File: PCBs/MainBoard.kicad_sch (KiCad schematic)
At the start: 47 parts, among them J1 USB_C_Receptacle, J2 Conn_01x12_FPC_0.5mm, J3 Conn_01x08, J4 Qwiic_RA, J5 SM06B-GHS-TB, SW1 PTH_RA_h7.5mm, SW2 SMD_4.6x2.8mm_h2.5mm, SW3 SMD_4.6x2.8mm_h2.5mm, U1 TVS_ESD_USB, U2 ESP32-S3-MINI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

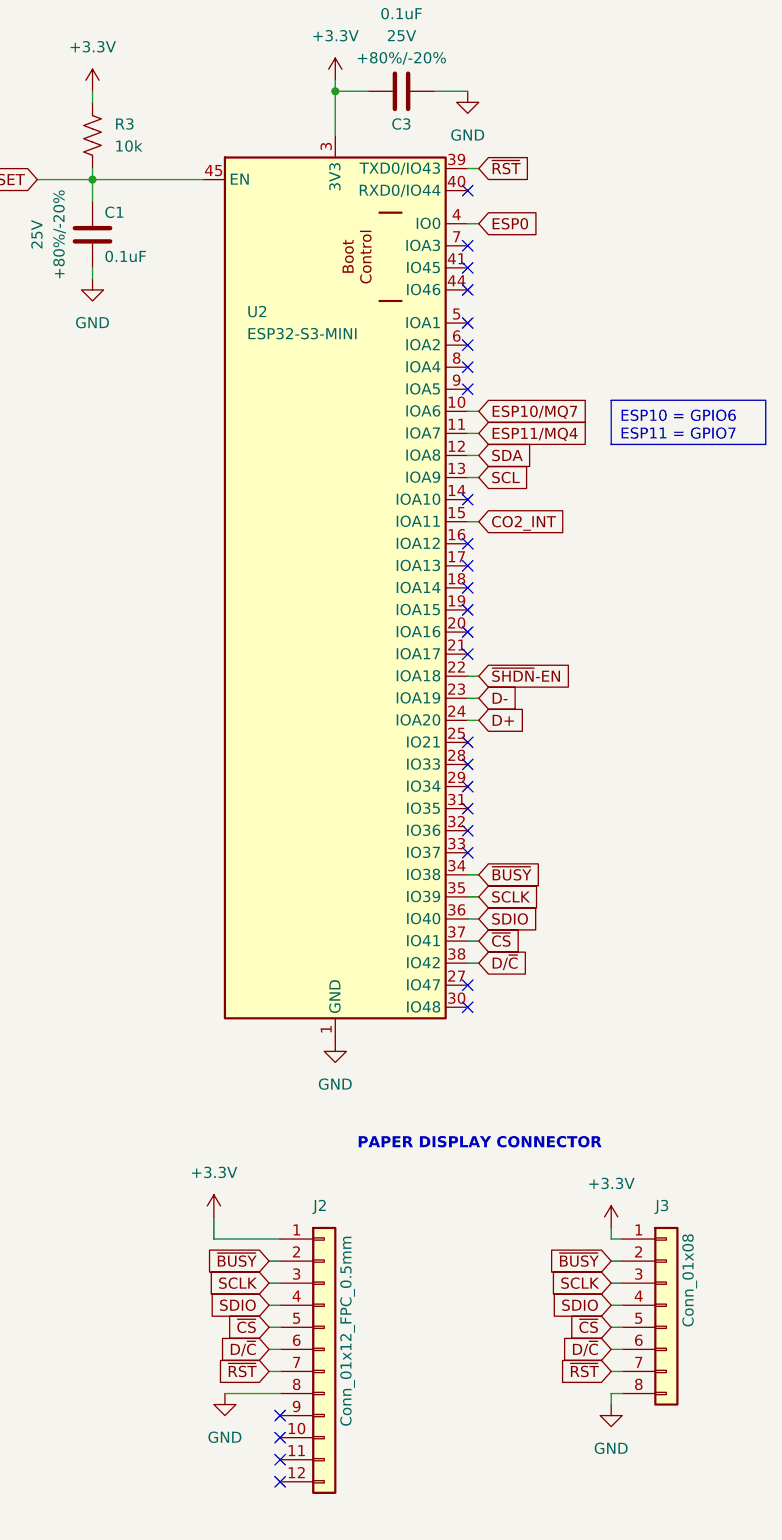
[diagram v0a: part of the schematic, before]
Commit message: Updates
Fixing connections between epaper display board and main board pcbs
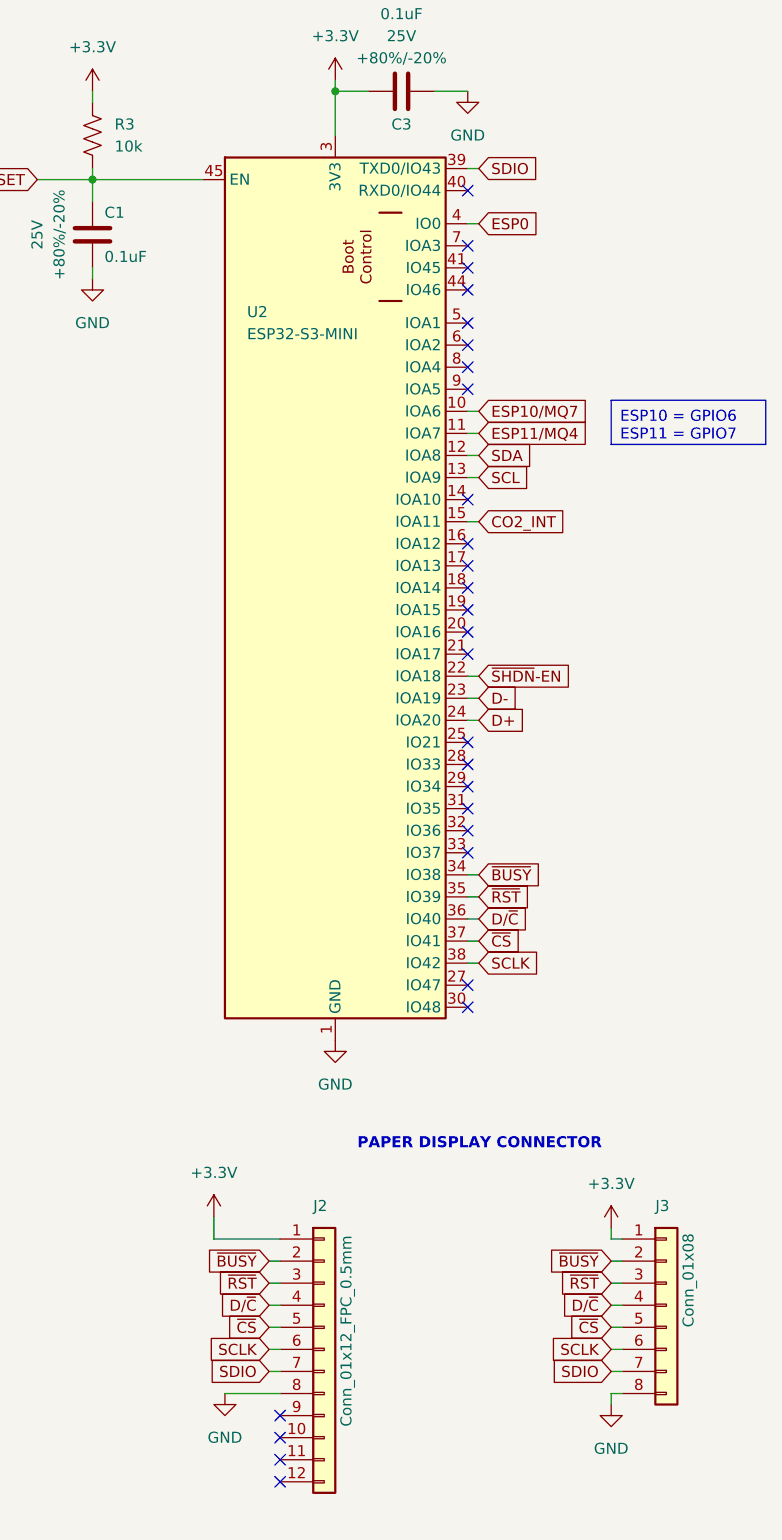
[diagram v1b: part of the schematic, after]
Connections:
- net D/~{C}: now also J2.4 (Pin_4), J3.4 (Pin_4), U2.36 (IO40); no longer J2.6 (Pin_6), J3.6 (Pin_6), U2.38 (IO42)
- net SCLK: now also J2.6 (Pin_6), J3.6 (Pin_6), U2.38 (IO42); no longer J2.3 (Pin_3), J3.3 (Pin_3), U2.35 (IO39)
- net SDIO: now also J2.7 (Pin_7), J3.7 (Pin_7), U2.39 (TXD0/IO43); no longer J2.4 (Pin_4), J3.4 (Pin_4), U2.36 (IO40)
- net ~{RST}: now also J2.3 (Pin_3), J3.3 (Pin_3), U2.35 (IO39); no longer J2.7 (Pin_7), J3.7 (Pin_7), U2.39 (TXD0/IO43)
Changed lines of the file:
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@@
+    )
+  )
+  (global_label "~{RST}" (shape input) (at 149.86 250.19 180) (fields_autoplaced)
+    (effects (font (size 1.27 1.27)) (justify right))
+    (property "Intersheetrefs" "${INTERSHEET_REFS}" (at 143.4277 250.19 0)
+      (effects (font (size 1.27 1.27)) (justify right) hide)
+    )
+  )
+  (global_label "SCLK" (shape input) (at 149.86 257.81 180) (fields_autoplaced)
+    (effects (font (size 1.27 1.27)) (justify right))
+    (property "Intersheetrefs" "${INTERSHEET_REFS}" (at 142.0972 257.81 0)
+      (effects (font (size 1.27 1.27)) (justify right) hide)
+    )
+  )
+  (global_label "D{slash}~{C}" (shape input) (at 134.62 208.28 0) (fields_autoplaced)
+    (effects (font (size 1.27 1.27)) (justify left))
+    (property "Intersheetrefs" "${INTERSHEET_REFS}" (at 141.4757 208.28 0)
+      (effects (font (size 1.27 1.27)) (justify left) hide)
     )
   )
@@
     )
   )
-  (global_label "SCLK" (shape input) (at 110.49 250.19 180) (fields_autoplaced)
-    (effects (font (size 1.27 1.27)) (justify right))
-    (property "Intersheetrefs" "${INTERSHEET_REFS}" (at 102.7272 250.19 0)
-      (effects (font (size 1.27 1.27)) (justify right) hide)
-    )
-  )
   (global_label "SDA" (shape input) (at 287.02 173.99 180) (fields_autoplaced)
     (effects (font (size 1.27 1.27)) (justify right))
@@
     )
   )
-  (global_label "SDIO" (shape input) (at 149.86 252.73 180) (fields_autoplaced)
-    (effects (font (size 1.27 1.27)) (justify right))
-    (property "Intersheetrefs" "${INTERSHEET_REFS}" (at 142.46 252.73 0)
-      (effects (font (size 1.27 1.27)) (justify right) hide)
-    )
-  )
-  (global_label "~{RST}" (shape input) (at 134.62 121.92 0) (fields_autoplaced)
-    (effects (font (size 1.27 1.27)) (justify left))
-    (property "Intersheetrefs" "${INTERSHEET_REFS}" (at 141.0523 121.92 0)
-      (effects (font (size 1.27 1.27)) (justify left) hide)
-    )
-  )
-  (global_label "SCLK" (shape input) (at 149.86 250.19 180) (fields_autoplaced)
-    (effects (font (size 1.27 1.27)) (justify right))
-    (property "Intersheetrefs" "${INTERSHEET_REFS}" (at 142.0972 250.19 0)
+  (global_label "SCLK" (shape input) (at 134.62 213.36 0) (fields_autoplaced)
+    (effects (font (size 1.27 1.27)) (justify left))
+    (property "Intersheetrefs" "${INTERSHEET_REFS}" (at 142.3828 213.36 0)
+      (effects (font (size 1.27 1.27)) (justify left) hide)
+    )
+  )
+  (global_label "SDIO" (shape input) (at 110.49 260.35 180) (fields_autoplaced)
+    (effects (font (size 1.27 1.27)) (justify right))
+    (property "Intersheetrefs" "${INTERSHEET_REFS}" (at 103.09 260.35 0)
       (effects (font (size 1.27 1.27)) (justify right) hide)
     )
@@
     )
   )
-  (global_label "D{slash}~{C}" (shape input) (at 134.62 213.36 0) (fields_autoplaced)
-    (effects (font (size 1.27 1.27)) (justify left))
-    (property "Intersheetrefs" "${INTERSHEET_REFS}" (at 141.4757 213.36 0)
+  (global_label "SDIO" (shape input) (at 134.62 121.92 0) (fields_autoplaced)
+    (effects (font (size 1.27 1.27)) (justify left))
+    (property "Intersheetrefs" "${INTERSHEET_REFS}" (at 142.02 121.92 0)
       (effects (font (size 1.27 1.27)) (justify left) hide)
     )
@@
     )
   )
-  (global_label "D{slash}~{C}" (shape input) (at 149.86 257.81 180) (fields_autoplaced)
-    (effects (font (size 1.27 1.27)) (justify right))
-    (property "Intersheetrefs" "${INTERSHEET_REFS}" (at 143.0043 257.81 0)
-      (effects (font (size 1.27 1.27)) (justify right) hide)
-    )
-  )
   (global_label "ESP0" (shape input) (at 134.62 128.27 0) (fields_autoplaced)
     (effects (font (size 1.27 1.27)) (justify left))
@@
     )
   )
+  (global_label "SCLK" (shape input) (at 110.49 257.81 180) (fields_autoplaced)
+    (effects (font (size 1.27 1.27)) (justify right))
+    (property "Intersheetrefs" "${INTERSHEET_REFS}" (at 102.7272 257.81 0)
+      (effects (font (size 1.27 1.27)) (justify right) hide)
+    )
+  )
+  (global_label "D{slash}~{C}" (shape input) (at 149.86 252.73 180) (fields_autoplaced)
+    (effects (font (size 1.27 1.27)) (justify right))
+    (property "Intersheetrefs" "${INTERSHEET_REFS}" (at 143.0043 252.73 0)
+      (effects (font (size 1.27 1.27)) (justify right) hide)
+    )
+  )
   (global_label "SCL" (shape input) (at 287.02 171.45 180) (fields_autoplaced)
     (effects (font (size 1.27 1.27)) (justify right))
@@
     )
   )
+  (global_label "~{RST}" (shape input) (at 134.62 205.74 0) (fields_autoplaced)
+    (effects (font (size 1.27 1.27)) (justify left))
+    (property "Intersheetrefs" "${INTERSHEET_REFS}" (at 141.0523 205.74 0)
+      (effects (font (size 1.27 1.27)) (justify left) hide)
+    )
+  )
   (global_label "RESET" (shape input) (at 40.64 135.89 0) (fields_autoplaced)
     (effects (font (size 1.27 1.27)) (justify left))
@@
     )
   )
-  (global_label "SCLK" (shape input) (at 134.62 205.74 0) (fields_autoplaced)
-    (effects (font (size 1.27 1.27)) (justify left))
-    (property "Intersheetrefs" "${INTERSHEET_REFS}" (at 142.3828 205.74 0)
-      (effects (font (size 1.27 1.27)) (justify left) hide)
-    )
-  )
   (global_label "CO2_INT" (shape input) (at 134.62 162.56 0) (fields_autoplaced)
     (effects (font (size 1.27 1.27)) (justify left))
@@
     )
   )
-  (global_label "SDIO" (shape input) (at 110.49 252.73 180) (fields_autoplaced)
-    (effects (font (size 1.27 1.27)) (justify right))
-    (property "Intersheetrefs" "${INTERSHEET_REFS}" (at 103.09 252.73 0)
-      (effects (font (size 1.27 1.27)) (justify right) hide)
-    )
-  )
   (global_label "SDA" (shape input) (at 134.62 154.94 0) (fields_autoplaced)
     (effects (font (size 1.27 1.27)) (justify left))
@@
     )
   )
+  (global_label "SDIO" (shape input) (at 149.86 260.35 180) (fields_autoplaced)
+    (effects (font (size 1.27 1.27)) (justify right))
+    (property "Intersheetrefs" "${INTERSHEET_REFS}" (at 142.46 260.35 0)
+      (effects (font (size 1.27 1.27)) (justify right) hide)
+    )
+  )
   (global_label "~{BUSY}" (shape input) (at 149.86 247.65 180) (fields_autoplaced)
     (effects (font (size 1.27 1.27)) (justify right))
@@
     )
   )
-  (global_label "D{slash}~{C}" (shape input) (at 110.49 257.81 180) (fields_autoplaced)
-    (effects (font (size 1.27 1.27)) (justify right))
-    (property "Intersheetrefs" "${INTERSHEET_REFS}" (at 103.6343 257.81 0)
-      (effects (font (size 1.27 1.27)) (justify right) hide)
-    )
-  )
   (global_label "~{CS}" (shape input) (at 134.62 210.82 0) (fields_autoplaced)
     (effects (font (size 1.27 1.27)) (justify left))
@@
     )
   )
-  (global_label "~{RST}" (shape input) (at 149.86 260.35 180) (fields_autoplaced)
-    (effects (font (size 1.27 1.27)) (justify right))
-    (property "Intersheetrefs" "${INTERSHEET_REFS}" (at 143.4277 260.35 0)
-      (effects (font (size 1.27 1.27)) (justify right) hide)
-    )
-  )
-  (global_label "~{RST}" (shape input) (at 110.49 260.35 180) (fields_autoplaced)
-    (effects (font (size 1.27 1.27)) (justify right))
-    (property "Intersheetrefs" "${INTERSHEET_REFS}" (at 104.0577 260.35 0)
-      (effects (font (size 1.27 1.27)) (justify right) hide)
-    )
-  )
-  (global_label "SDIO" (shape input) (at 134.62 208.28 0) (fields_autoplaced)
-    (effects (font (size 1.27 1.27)) (justify left))
-    (property "Intersheetrefs" "${INTERSHEET_REFS}" (at 142.02 208.28 0)
-      (effects (font (size 1.27 1.27)) (justify left) hide)
+  (global_label "D{slash}~{C}" (shape input) (at 110.49 252.73 180) (fields_autoplaced)
+    (effects (font (size 1.27 1.27)) (justify right))
+    (property "Intersheetrefs" "${INTERSHEET_REFS}" (at 103.6343 252.73 0)
+      (effects (font (size 1.27 1.27)) (justify right) hide)
     )
   )
@@
     )
   )
+  (global_label "~{RST}" (shape input) (at 110.49 250.19 180) (fields_autoplaced)
+    (effects (font (size 1.27 1.27)) (justify right))
+    (property "Intersheetrefs" "${INTERSHEET_REFS}" (at 104.0577 250.19 0)
+      (effects (font (size 1.27 1.27)) (justify right) hide)
+    )
+  )

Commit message: Main PCB update
Updated per comments in google doc
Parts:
- removed J5: SM06B-GHS-TB, CONN_SM06B-GHS-TB_JST, symbol SM06B-GHS-TB:SM06B-GHS-TB
- added FID1, FID2, FID3, FID4: Fiducial_0.5mm, SparkFun-Aesthetic:Fiducial_0.5mm_Mask1mm, symbol SparkFun-Aesthetic:Fiducial_0.5mm
- added G2: SparkFun_Logo, symbol SparkFun-Aesthetic:SparkFun_Logo
- added ST1: Stand_off, SparkFun-Hardware:STAND-OFF, symbol SparkFun-Hardware:Stand_off
- added U8: SEN54, SparkFun-Connector:JST-6-SMD-1.25MM-LOCKING, symbol SparkFun-Sensor:SEN55
- J2: PROD_ID (none) -> CONN-15766
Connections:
- net +5V: now also U8.1 (VDD)
- net GND: now also U8.2 (GND), U8.5 (SEL)
- net SCL: now also U8.4 (SCL)
- net SDA: now also U8.3 (SDA)
- no-connect marks 32 -> 31
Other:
- note added: "Fiducials"
- note added: "SEN55 CONNECTOR"
- note added: "Stand Off"
- note added: "Topside Right Topside left Bottomside Right Bottomside left"
- note removed: "SEN54 CONNECTOR"

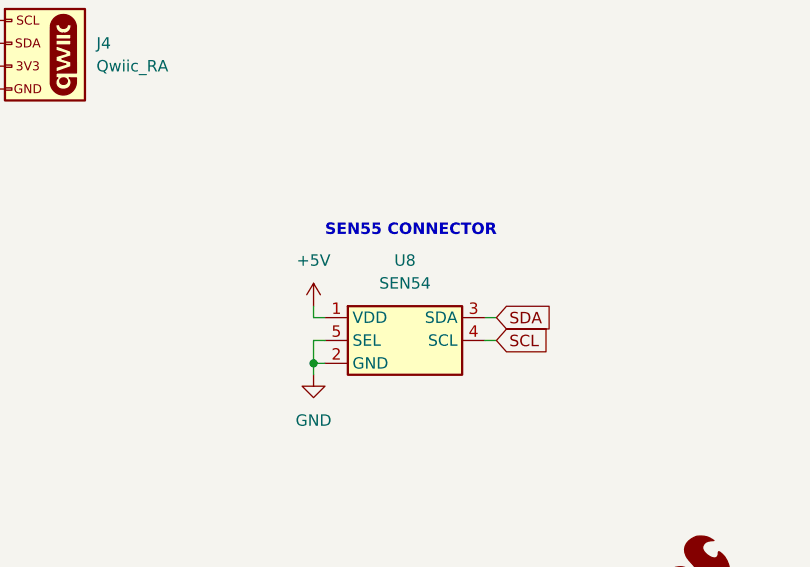
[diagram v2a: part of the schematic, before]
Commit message: Updated SEN55
Brought back the SEN55 to the board
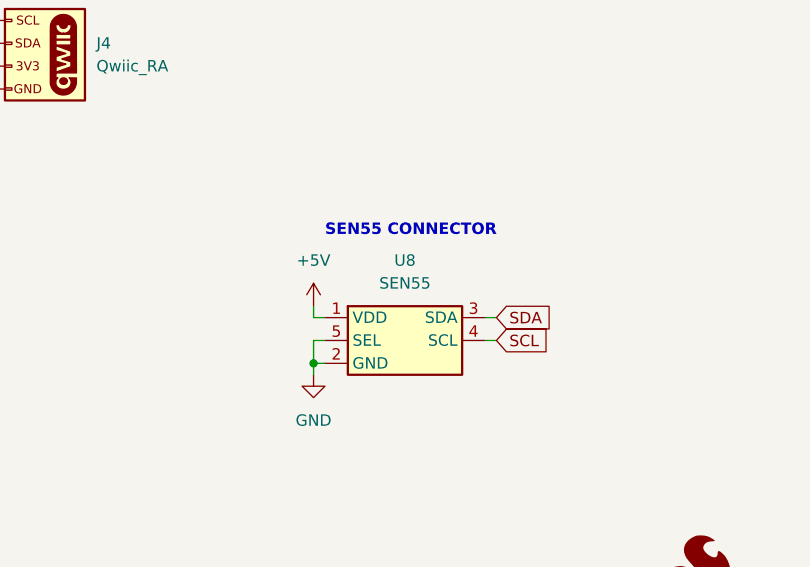
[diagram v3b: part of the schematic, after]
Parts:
- U8: value SEN54 -> SEN55; PROD_ID SUB-16569 -> IC-21278
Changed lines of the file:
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@@
+    )
+  )
+  (symbol (lib_id "SparkFun-Sensor:SEN55") (at 356.87 207.01 0) (unit 1)
+    (in_bom yes) (on_board yes) (dnp no) (fields_autoplaced)
+    (property "Reference" "U8" (at 356.87 198.12 0)
+      (effects (font (size 1.27 1.27)))
+    )
+    (property "Value" "SEN55" (at 356.87 200.66 0)
+      (effects (font (size 1.27 1.27)))
+    )
+    (property "Footprint" "SparkFun-Connector:JST-6-SMD-1.25MM-LOCKING" (at 354.965 215.9 0)
+      (effects (font (size 1.27 1.27) italic) hide)
+    )
+    (property "Datasheet" "https://cdn.sparkfun.com/assets/b/0/3/c/0/Sensirion_Datasheet_Environmental_Node_SEN5x.pdf" (at 360.68 218.44 0)
+      (effects (font (size 1.27 1.27)) hide)
+    )
+    (property "PROD_ID" "IC-21278" (at 356.87 213.36 0)
+      (effects (font (size 1.27 1.27)) hide)
+    )
+    (pin "1")
+    (pin "2")
+    (pin "3")
+    (pin "4")
+    (pin "5")
+    (pin "6")
+    (instances
+      (project "MainBoard"
+        (path "/70111962-74ad-442f-8642-d12c4115fcfb"
+          (reference "U8") (unit 1)
+        )
+      )
     )
   )
@@
         )
       )
-    )
-  )
-  (symbol (lib_id "SparkFun-Sensor:SEN55") (at 356.87 207.01 0) (unit 1)
-    (in_bom yes) (on_board yes) (dnp no) (fields_autoplaced)
-    (property "Reference" "U8" (at 356.87 198.12 0)
-      (effects (font (size 1.27 1.27)))
-    )
-    (property "Value" "SEN54" (at 356.87 200.66 0)
-      (effects (font (size 1.27 1.27)))
-    )
-    (property "Footprint" "SparkFun-Connector:JST-6-SMD-1.25MM-LOCKING" (at 354.965 215.9 0)
-      (effects (font (size 1.27 1.27) italic) hide)
-    )
-    (property "Datasheet" "https://cdn.sparkfun.com/assets/b/0/3/c/0/Sensirion_Datasheet_Environmental_Node_SEN5x.pdf" (at 360.68 218.44 0)
-      (effects (font (size 1.27 1.27)) hide)
-    )
-    (property "PROD_ID" "SUB-16569" (at 356.87 213.36 0)
-      (effects (font (size 1.27 1.27)) hide)
-    )
-    (pin "1")
-    (pin "2")
-    (pin "3")
-    (pin "4")
-    (pin "5")
-    (pin "6")
-    (instances
-      (project "MainBoard"
-        (path "/70111962-74ad-442f-8642-d12c4115fcfb"
-          (reference "U8") (unit 1)
-        )
-      )

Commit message: Main Board PCB update
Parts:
- added C13, C14: 10uF, SparkFun-Capacitor:C_0603_1608Metric, symbol SparkFun-Capacitor:10uF_0603_10V_20%
- added Q1: AO3404A, SparkFun-Semiconductor-Standard:SOT23-3, symbol SparkFun-DiscreteSemi:Q_NMOS_5.8A_30V
- added R13: 10k, SparkFun-Resistor:R_0603_1608Metric, symbol SparkFun-Resistor:10k_0603
- added R14: 1k, SparkFun-Resistor:R_0603_1608Metric, symbol SparkFun-Resistor:1k_0603
- added U9: MQ-7 Gas Sensor, SparkFun-Sensor:MQ-7 Gas Sensor, symbol SparkFun-Sensor:MQ-7_Gas_Sensor_-_Full_Pinout
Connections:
- net +5V: now also U9.4 (GND), U9.6 (GND)
- net GND: now also R13.2
- new net: R13.1, U9.1 (SENSE), U9.3 (SENSE)
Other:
- note added: "CO SENSOR"
- note added: "METHANE SENSOR"
- note added: "PASCO2 CIRCUIT"
- note added: "QWIIC CONNECTOR CIRCUIT"
- moved on the sheet: R11, U7
